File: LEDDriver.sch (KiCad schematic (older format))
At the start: 0 parts

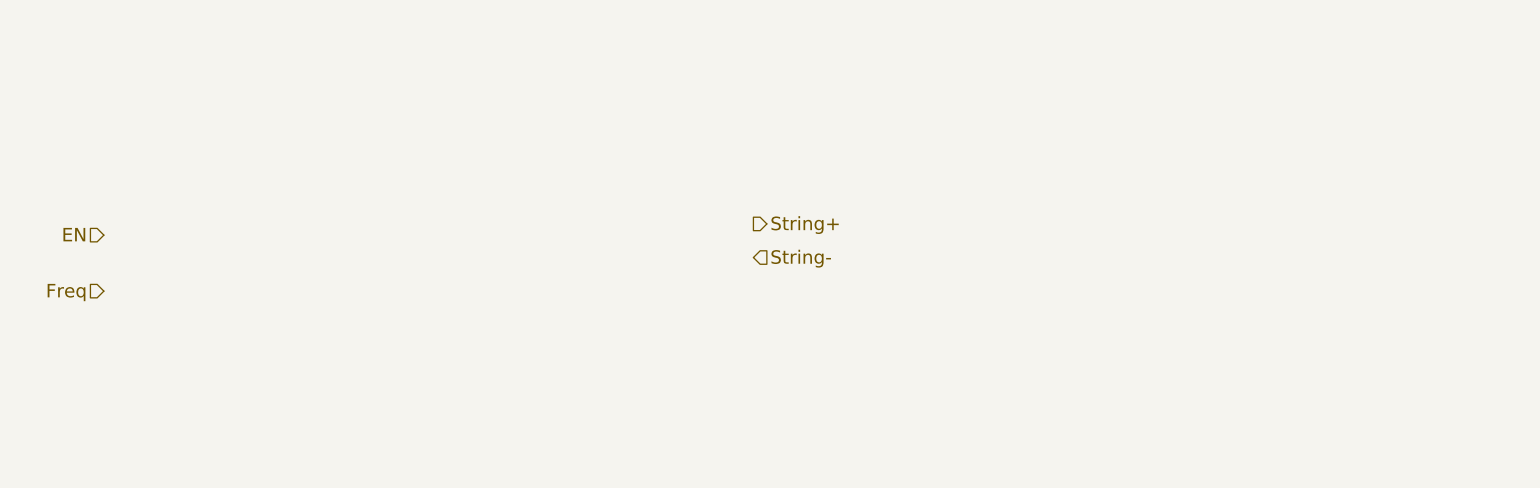
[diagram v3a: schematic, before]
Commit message: LED driver model
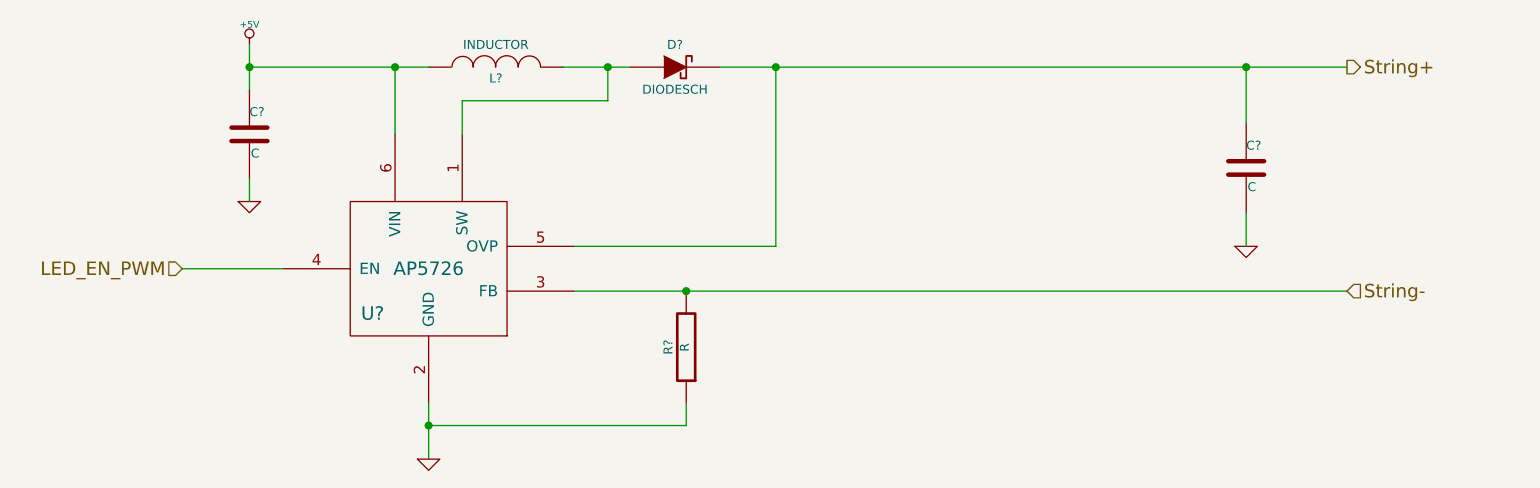
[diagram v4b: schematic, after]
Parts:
- added C? (x2): C, ~, symbol C
- added D?: DIODESCH, ~, symbol DIODESCH
- added L?: INDUCTOR, ~, symbol INDUCTOR
- added R?: R, ~, symbol R
- added U?: AP5726, symbol AP5726
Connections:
- net String+: now also C?.1, D?.2 (K), U?.5 (OVP)
- net String-: now also R?.2, U?.3 (FB)
- new net: D?.1 (A), L?.2, U?.1 (SW)
- new net +5V: C?.1, L?.1, U?.6 (VIN)
- new net GND: C?.2, C?.2, R?.1, U?.2 (GND)
- new net LED_EN_PWM: U?.4 (EN)
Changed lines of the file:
@@
 Sheet 6 9
 Title ""
-Date "29 sep 2013"
+Date "30 sep 2013"
 Rev ""
 Comp ""
@@
 Comment4 ""
 $EndDescr
-Text HLabel 2650 2100 0    60   Input ~ 0
-EN
-Text HLabel 2650 2350 0    60   Input ~ 0
-Freq
-Text HLabel 5550 2050 2    60   Output ~ 0
+Text HLabel 3000 2250 0    60   Input ~ 0
+LED_EN_PWM
+Text HLabel 8200 1350 2    60   Output ~ 0
 String+
-Text HLabel 5550 2200 2    60   Input ~ 0
+Text HLabel 8200 2350 2    60   Input ~ 0
 String-
+$Comp
+L AP5726 U?
+U 1 1 52497097
+P 4100 2250
+F 0 "U?" H 3850 2050 60  0000 C CNN
+F 1 "AP5726" H 4100 2250 60  0000 C CNN
+F 2 "" H 4100 2050 60  0000 C CNN
+F 3 "" H 4100 2050 60  0000 C CNN
+	1    4100 2250
+	1    0    0    -1
+$EndComp
+Wire Wire Line
+	3000 2250 3450 2250
+$Comp
+L GND #PWR?
+U 1 1 524970AC
+P 4100 3100
+F 0 "#PWR?" H 4100 3100 30  0001 C CNN
+F 1 "GND" H 4100 3030 30  0001 C CNN
+F 2 "" H 4100 3100 60  0000 C CNN
+F 3 "" H 4100 3100 60  0000 C CNN
+	1    4100 3100
+	1    0    0    -1
+$EndComp
+Wire Wire Line
+	4100 2850 4100 2950
+Wire Wire Line
+	4100 2950 4100 3100
+$Comp
+L +5V #PWR?
+U 1 1 524972CC
+P 3300 1250
+F 0 "#PWR?" H 3300 1340 20  0001 C CNN
+F 1 "+5V" H 3300 1340 30  0000 C CNN
+F 2 "" H 3300 1250 60  0000 C CNN
+F 3 "" H 3300 1250 60  0000 C CNN
+	1    3300 1250
+	1    0    0    -1
+$EndComp
+$Comp
+L GND #PWR?
+U 1 1 524972D9
+P 3300 1950
+F 0 "#PWR?" H 3300 1950 30  0001 C CNN
+F 1 "GND" H 3300 1880 30  0001 C CNN
+F 2 "" H 3300 1950 60  0000 C CNN
+F 3 "" H 3300 1950 60  0000 C CNN
+	1    3300 1950
+	1    0    0    -1
+$EndComp
+$Comp
+L C C?
+U 1 1 524972EB
+P 3300 1650
+F 0 "C?" H 3300 1750 40  0000 L CNN
+F 1 "C" H 3306 1565 40  0000 L CNN
+F 2 "~" H 3338 1500 30  0000 C CNN
+F 3 "~" H 3300 1650 60  0000 C CNN
+	1    3300 1650
+	1    0    0    -1
+$EndComp
+Wire Wire Line
+	3300 1250 3300 1350
+Wire Wire Line
+	3300 1350 3300 1450
+Wire Wire Line
+	3300 1850 3300 1950
+Wire Wire Line
+	3300 1350 3950 1350
+Wire Wire Line
+	3950 1350 4100 1350
+Wire Wire Line
+	3950 1350 3950 1650
+Connection ~ 3300 1350
+$Comp
+L C C?
+U 1 1 52497315
+P 7750 1800
+F 0 "C?" H 7750 1900 40  0000 L CNN
+F 1 "C" H 7756 1715 40  0000 L CNN
+F 2 "~" H 7788 1650 30  0000 C CNN
+F 3 "~" H 7750 1800 60  0000 C CNN
+	1    7750 1800
+	1    0    0    -1
+$EndComp
+$Comp
+L INDUCTOR L?
+U 1 1 5249731D
+P 4400 1350
+F 0 "L?" V 4350 1350 40  0000 C CNN
+F 1 "INDUCTOR" V 4500 1350 40  0000 C CNN
+F 2 "~" H 4400 1350 60  0000 C CNN
+F 3 "~" H 4400 1350 60  0000 C CNN
+	1    4400 1350
+	0    -1   -1   0
+$EndComp
+Connection ~ 3950 1350
+Wire Wire Line
+	4250 1650 4250 1500
+Wire Wire Line
+	4250 1500 4900 1500
+Wire Wire Line
+	4900 1500 4900 1350
+Wire Wire Line
+	4700 1350 4900 1350
+Wire Wire Line
+	4900 1350 5000 1350
+$Comp
+L DIODESCH D?
+U 1 1 5249733F
+P 5200 1350
+F 0 "D?" H 5200 1450 40  0000 C CNN
+F 1 "DIODESCH" H 5200 1250 40  0000 C CNN
+F 2 "~" H 5200 1350 60  0000 C CNN
+F 3 "~" H 5200 1350 60  0000 C CNN
+	1    5200 1350
+	1    0    0    -1
+$EndComp
+Connection ~ 4900 1350
+Wire Wire Line
+	5400 1350 5650 1350
+Wire Wire Line
+	5650 1350 7750 1350
+Wire Wire Line
+	7750 1350 8200 1350
+Wire Wire Line
+	7750 1350 7750 1600
+$Comp
+L GND #PWR?
+U 1 1 52497391
+P 7750 2150
+F 0 "#PWR?" H 7750 2150 30  0001 C CNN
+F 1 "GND" H 7750 2080 30  0001 C CNN
+F 2 "" H 7750 2150 60  0000 C CNN
+F 3 "" H 7750 2150 60  0000 C CNN
+	1    7750 2150
+	1    0    0    -1
+$EndComp
+Connection ~ 7750 1350
+Wire Wire Line
+	7750 2150 7750 2000
+Wire Wire Line
+	4750 2150 5650 2150
+Wire Wire Line
+	5650 2150 5650 1350
+Connection ~ 5650 1350
+$Comp
+L R R?
+U 1 1 524973D0
+P 5250 2600
+F 0 "R?" V 5330 2600 40  0000 C CNN
+F 1 "R" V 5257 2601 40  0000 C CNN
+F 2 "~" V 5180 2600 30  0000 C CNN
+F 3 "~" H 5250 2600 30  0000 C CNN
+	1    5250 2600
+	-1   0    0    1
+$EndComp
+Wire Wire Line
+	5250 2850 5250 2950
+Wire Wire Line
+	5250 2950 4100 2950
+Connection ~ 4100 2950
+Wire Wire Line
+	4750 2350 5250 2350
+Wire Wire Line
+	5250 2350 8200 2350
+Connection ~ 5250 2350
 $EndSCHEMATC

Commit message: Arduino Module
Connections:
- net String+ renamed LED_STRING+
- net String- renamed LED_STRING-
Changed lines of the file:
@@
 LED_EN_PWM
 Text HLabel 8200 1350 2    60   Output ~ 0
-String+
+LED_STRING+
 Text HLabel 8200 2350 2    60   Input ~ 0
-String-
+LED_STRING-
 $Comp
 L AP5726 U?
